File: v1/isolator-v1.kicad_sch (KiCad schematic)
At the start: 43 parts, among them J1 HOST, J2 PORT, Q1 2N7002, T1 750313638, U1 ADuM4165, U2 USBLC6-2SC6, U3 USBLC6-2SC6, U4 SN6505BDBV, U5 TLV76750DGNR, U6 TPS2553DBV, Y1 24M 8pF

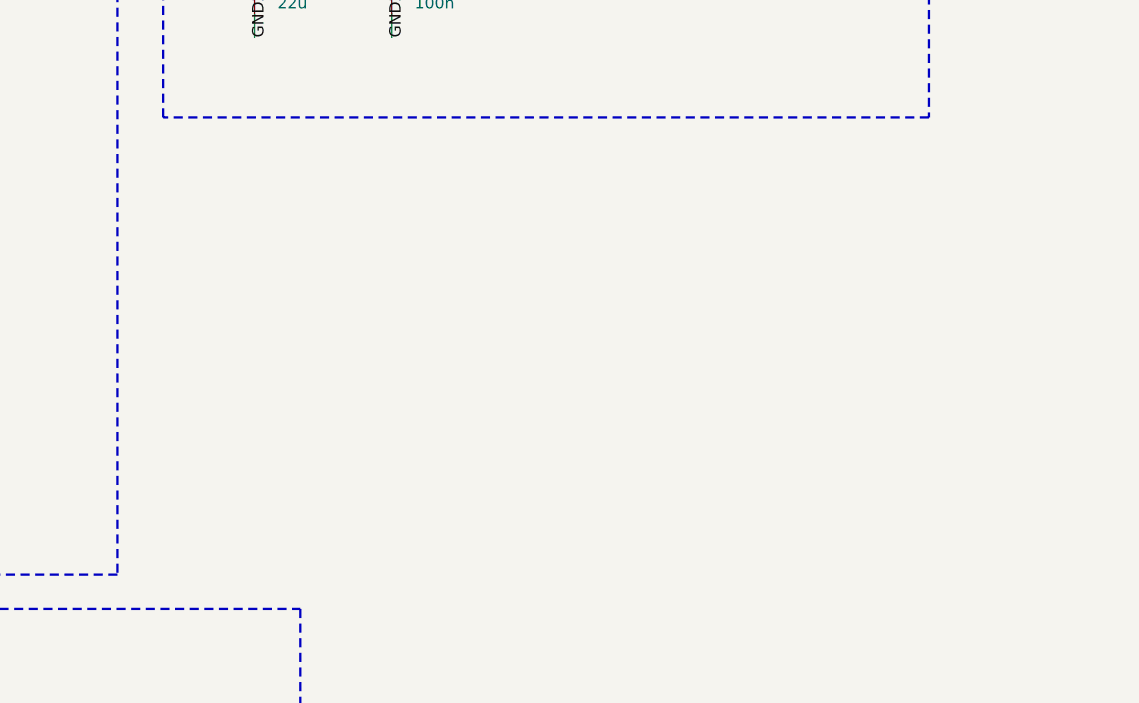
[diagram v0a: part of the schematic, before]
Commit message: feat(v1/sch): footprint audit and binding layout constraints (Task 7)
Audited all 43 v1 component instances: every symbol already carried the
correct footprint from Tasks 2-6 (no reassignment needed). Verified all 15
distinct footprints resolve to real files on disk (stock KiCad libraries +
isolator-lib.pretty), not just non-empty strings.

Added the "V1 LAYOUT CONSTRAINTS -- BINDING" text block to previously-empty
sheet space so the PCB plan inherits the 7 binding constraints (edge
pullback, ESD placement, barrier creepage, bypass lead length, connector
mounting, and the 1.7 mm length-chain margin / D1+D2 side-by-side
requirement) without needing the spec open.

Mechanical sanity check against the Task 1 feasibility budget found the
rectifier zone's real margin is +0.64 mm, not the +2.64 mm previously
reported -- the feasibility doc's D_SMA dimension was an unmeasured 5.0 mm
placeholder; the real D_SMA footprint is 7.0 mm along the load-bearing
axis. Still GO, but effectively zero slack; flagged for Task 8, no
schematic change needed since the footprint is correct.

Verified: ERC baseline held (0 errors, 1 pre-existing lib_symbol_mismatch
warning on U4), netlist MISSING FOOTPRINTS none, programmatic overlap
sweep (124 text/label items) clean, visual render clean.

Co-Authored-By: Claude Opus 5 <noreply@anthropic.com>
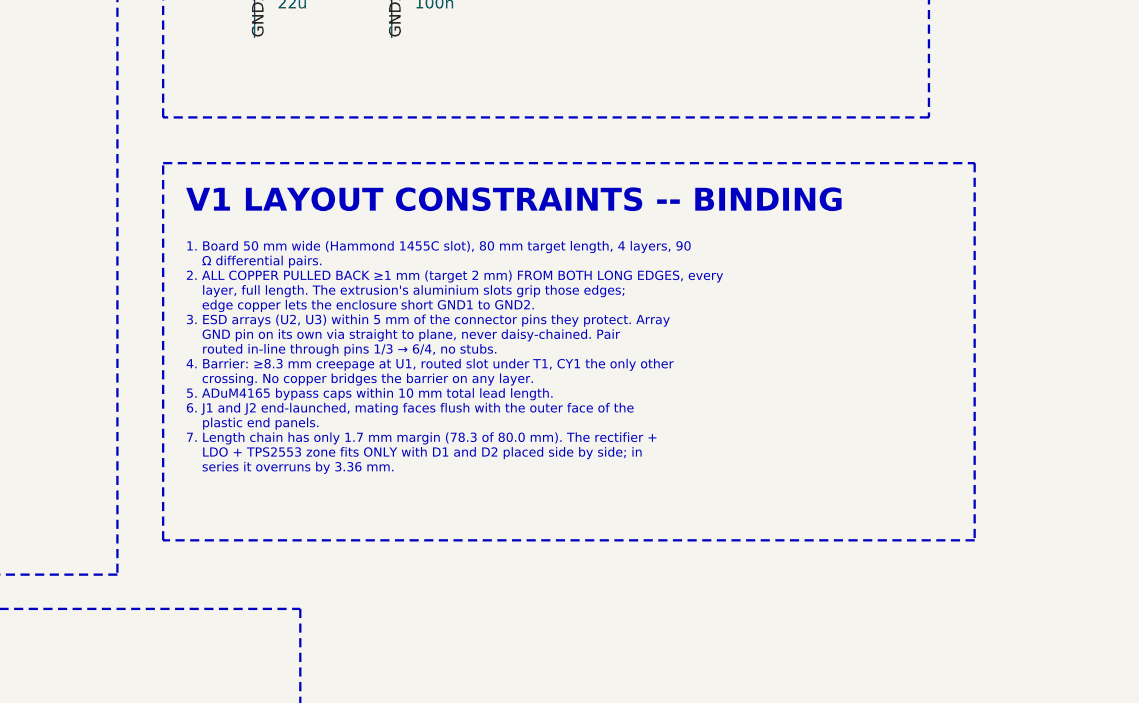
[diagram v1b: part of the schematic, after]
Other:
- note added: "1. Board 50 mm wide (Hammond 1455C slot), 80 mm target length, 4 layers, 90 Ω differential pairs. 2. ALL COPPER PULLED BACK ≥1 mm (target 2 mm) FROM BOTH LONG EDGES, every layer, full length. The extrusion's aluminium slots grip those edges; edge copper lets the enclosure short GND1 to GND2. 3. ESD arrays (U2, U3) within 5 mm of the connector pins they protect. Array GND pin on its own via straig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"
- note added: "V1 LAYOUT CONSTRAINTS -- BINDING"
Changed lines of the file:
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@@
+		)
+	)
+	(rectangle
+		(start 314.96 190.5)
+		(end 405.13 232.41)
+		(stroke
+			(width 0.254)
+			(type dash)
+		)
+		(fill
+			(type none)
+		)
+	)
+	(text "V1 LAYOUT CONSTRAINTS -- BINDING"
+		(exclude_from_sim no)
+		(at 317.5 196.34 0)
+		(effects
+			(font
+				(size 2.54 2.54)
+				(bold yes)
+			)
+			(justify left bottom)
+		)
+	)
+	(text "1. Board 50 mm wide (Hammond 1455C slot), 80 mm target length, 4 layers, 90\n    Ω differential pairs.\n2. ALL COPPER PULLED BACK ≥1 mm (target 2 mm) FROM BOTH LONG EDGES, every\n    layer, full length. The extrusion's aluminium slots grip those edges;\n    edge copper lets the enclosure short GND1 to GND2.\n3. ESD arrays (U2, U3) within 5 mm of the connector pins they protect. Array\n    GND pin on its own via straight to plane, never daisy-chained. Pair\n    routed in-line through pins 1/3 → 6/4, no stubs.\n4. Barrier: ≥8.3 mm creepage at U1, routed slot under T1, CY1 the only other\n    crossing. No copper bridges the barrier on any layer.\n5. ADuM4165 bypass caps within 10 mm total lead length.\n6. J1 and J2 end-launched, mating faces flush with the outer face of the\n    plastic end panels.\n7. Length chain has only 1.7 mm margin (78.3 of 80.0 mm). The rectifier +\n    LDO + TPS2553 zone fits ONLY with D1 and D2 placed side by side; in\n    series it overruns by 3.36 mm."
+		(exclude_from_sim no)
+		(at 317.5 199.39 0)
+		(effects
+			(font
+				(size 1.016 1.016)
+			)
+			(justify left top)
 		)
 	)

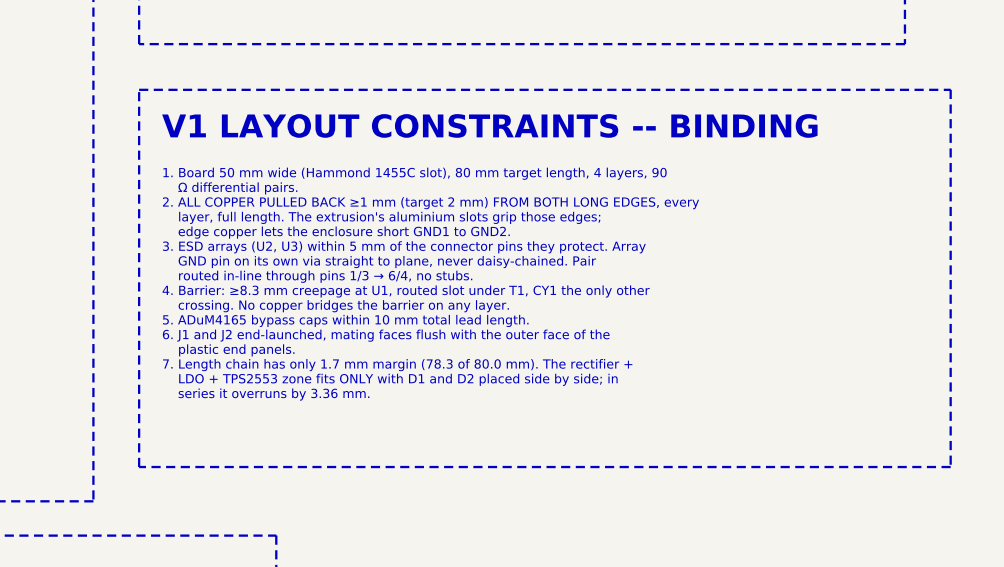
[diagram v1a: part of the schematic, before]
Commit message: docs(v1): move feasibility record to 1455C1202, fix utilization arithmetic (Task 7 fix round 1)
Human partner ruled v1 moves to the 1455C1202 (120 mm) enclosure after the
reviewer extended Task 7's own recompute methodology to zones 1/5 and found
the full 5-zone chain no longer closes against 80 mm (80.1-83.7 mm real vs
80.0 mm available). Spec/plan already updated in 7366d81.

- Schematic constraints text (v1/isolator-v1.kicad_sch): item 1 now reads
  "120 mm length (1455C1202)"; item 7 rewritten to drop the stale 1.7 mm
  margin figure and carry forward only what survives the enclosure change
  -- the rectifier zone measures 19.36 mm and D1/D2 must be placed side by
  side, not in series. Text-only edit, netlist unchanged (verified by diff).

- docs/superpowers/reviews/2026-07-28-v1-mechanical-feasibility.md rewritten
  in full: 120 mm/5520 mm^2 envelope, every one of the 43 BOM components
  measured individually (zero placeholders anywhere, 921.98 mm^2 total,
  16.7% utilization), 5-zone chain recomputed for zones 1/4/5 (80.10-83.70
  mm, reproducing the review's own numbers), zone 2 flagged as a conservative
  hold rather than a re-derived figure, and the 1-D-chain-vs-2-D-board
  caveat carried through so this isn't written up as a hard 80 mm failure.

- Utilization arithmetic error corrected and explained: the previous
  919.6 mm^2/25.0% figure mixed measured and placeholder values
  inconsistently without saying so. Reproduced the review's clean partial
  reconstruction (871.9 mm^2/23.7%) to show where it came from, then
  superseded both with a from-scratch, zero-placeholder recompute.

Re-verified: ERC baseline held (0 errors, 1 pre-existing lib_symbol_mismatch
on U4), netlist identical apart from export timestamp, overlap sweep clean
(124 items), 300 dpi render clean.

Co-Authored-By: Claude Opus 5 <noreply@anthropic.com>
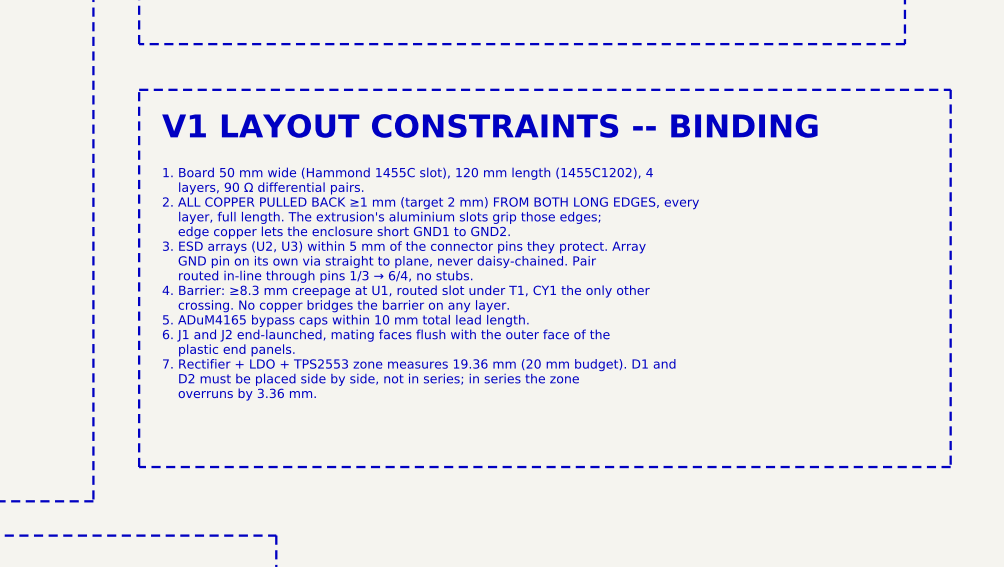
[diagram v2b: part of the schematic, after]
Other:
- note added: "1. Board 50 mm wide (Hammond 1455C slot), 120 mm length (1455C1202), 4 layers, 90 Ω differential pairs. 2. ALL COPPER PULLED BACK ≥1 mm (target 2 mm) FROM BOTH LONG EDGES, every layer, full length. The extrusion's aluminium slots grip those edges; edge copper lets the enclosure short GND1 to GND2. 3. ESD arrays (U2, U3) within 5 mm of the connector pins they protect. Array GND pin on its own via 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"
- note removed: "1. Board 50 mm wide (Hammond 1455C slot), 80 mm target length, 4 layers, 90 Ω differential pairs. 2. ALL COPPER PULLED BACK ≥1 mm (target 2 mm) FROM BOTH LONG EDGES, every layer, full length. The extrusion's aluminium slots grip those edges; edge copper lets the enclosure short GND1 to GND2. 3. ESD arrays (U2, U3) within 5 mm of the connector pins they protect. Array GND pin on its own via straig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"
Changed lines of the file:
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@@
 		)
 	)
-	(text "1. Board 50 mm wide (Hammond 1455C slot), 80 mm target length, 4 layers, 90\n    Ω differential pairs.\n2. ALL COPPER PULLED BACK ≥1 mm (target 2 mm) FROM BOTH LONG EDGES, every\n    layer, full length. The extrusion's aluminium slots grip those edges;\n    edge copper lets the enclosure short GND1 to GND2.\n3. ESD arrays (U2, U3) within 5 mm of the connector pins they protect. Array\n    GND pin on its own via straight to plane, never daisy-chained. Pair\n    routed in-line through pins 1/3 → 6/4, no stubs.\n4. Barrier: ≥8.3 mm creepage at U1, routed slot under T1, CY1 the only other\n    crossing. No copper bridges the barrier on any layer.\n5. ADuM4165 bypass caps within 10 mm total lead length.\n6. J1 and J2 end-launched, mating faces flush with the outer face of the\n    plastic end panels.\n7. Length chain has only 1.7 mm margin (78.3 of 80.0 mm). The rectifier +\n    LDO + TPS2553 zone fits ONLY with D1 and D2 placed side by side; in\n    series it overruns by 3.36 mm."
+	(text "1. Board 50 mm wide (Hammond 1455C slot), 120 mm length (1455C1202), 4\n    layers, 90 Ω differential pairs.\n2. ALL COPPER PULLED BACK ≥1 mm (target 2 mm) FROM BOTH LONG EDGES, every\n    layer, full length. The extrusion's aluminium slots grip those edges;\n    edge copper lets the enclosure short GND1 to GND2.\n3. ESD arrays (U2, U3) within 5 mm of the connector pins they protect. Array\n    GND pin on its own via straight to plane, never daisy-chained. Pair\n    routed in-line through pins 1/3 → 6/4, no stubs.\n4. Barrier: ≥8.3 mm creepage at U1, routed slot under T1, CY1 the only other\n    crossing. No copper bridges the barrier on any layer.\n5. ADuM4165 bypass caps within 10 mm total lead length.\n6. J1 and J2 end-launched, mating faces flush with the outer face of the\n    plastic end panels.\n7. Rectifier + LDO + TPS2553 zone measures 19.36 mm (20 mm budget). D1 and\n    D2 must be placed side by side, not in series; in series the zone\n    overruns by 3.36 mm."
 		(exclude_from_sim no)
 		(at 317.5 199.39 0)

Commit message: feat(v1/sch): MPNs, BOM export, schematic design review
Closes the two named BOM gaps (C3/C7 4.7uF, C8/C10 47uF) with live-verified
LCSC parts, and verifies R3-R8/R9/R10/U5 LCSC codes against the live
catalogue. Exports the BOM (25 lines, 100% MPN coverage), runs the
kicad-happy analyzer, and walks the v1 spec point by point against the
exported netlist (8/8 satisfied, 0 deviations). All 6 non-info analyzer
findings triaged as false positives of one root cause (PWR_FLAG not
recognized as a net source), already identified and accepted in Task 6.
ERC unchanged from baseline: 0 errors, 1 pre-existing lib_symbol_mismatch
warning on U4, not touched per prior direction.

Co-Authored-By: Claude Opus 5 <noreply@anthropic.com>
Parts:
- C10, C8: LCSC (none) -> C90142; MPN (none) -> TMK325ABJ476MM-P; Manufacturer (none) -> Taiyo Yuden
- C3, C7: LCSC (none) -> C162427; MPN (none) -> GRM21BR71E475KA73L; Manufacturer (none) -> Murata
- R10, R4, R9: LCSC (none) -> C14675
- R3: LCSC (none) -> C273780
- R5: LCSC (none) -> C105881
- R6: LCSC (none) -> C137732
- R7, R8: LCSC (none) -> C114630
- U5: LCSC (none) -> C3752807
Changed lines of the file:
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@@
 			)
 		)
+		(property "MPN" "GRM21BR71E475KA73L"
+			(at 25.4 49.53 0)
+			(show_name no)
+			(do_not_autoplace no)
+		(hide yes)
+			(effects
+				(font
+					(size 1.27 1.27)
+				)
+			)
+		)
+		(property "Manufacturer" "Murata"
+			(at 25.4 49.53 0)
+			(show_name no)
+			(do_not_autoplace no)
+		(hide yes)
+			(effects
+				(font
+					(size 1.27 1.27)
+				)
+			)
+		)
+		(property "LCSC" "C162427"
+			(at 25.4 49.53 0)
+			(show_name no)
+			(do_not_autoplace no)
+		(hide yes)
+			(effects
+				(font
+					(size 1.27 1.27)
+				)
+			)
+		)
 		(pin "1"
 		)
@@
 			)
 		)
+		(property "MPN" "GRM21BR71E475KA73L"
+			(at 38.1 130.81 0)
+			(show_name no)
+			(do_not_autoplace no)
+		(hide yes)
+			(effects
+				(font
+					(size 1.27 1.27)
+				)
+			)
+		)
+		(property "Manufacturer" "Murata"
+			(at 38.1 130.81 0)
+			(show_name no)
+			(do_not_autoplace no)
+		(hide yes)
+			(effects
+				(font
+					(size 1.27 1.27)
+				)
+			)
+		)
+		(property "LCSC" "C162427"
+			(at 38.1 130.81 0)
+			(show_name no)
+			(do_not_autoplace no)
+		(hide yes)
+			(effects
+				(font
+					(size 1.27 1.27)
+				)
+			)
+		)
 		(pin "1"
 		)
@@
 			)
 		)
+		(property "MPN" "TMK325ABJ476MM-P"
+			(at 222.25 135.89 0)
+			(show_name no)
+			(do_not_autoplace no)
+		(hide yes)
+			(effects
+				(font
+					(size 1.27 1.27)
+				)
+			)
+		)
+		(property "Manufacturer" "Taiyo Yuden"
+			(at 222.25 135.89 0)
+			(show_name no)
+			(do_not_autoplace no)
+		(hide yes)
+			(effects
+				(font
+					(size 1.27 1.27)
+				)
+			)
+		)
+		(property "LCSC" "C90142"
+			(at 222.25 135.89 0)
+			(show_name no)
+			(do_not_autoplace no)
+		(hide yes)
+			(effects
+				(font
+					(size 1.27 1.27)
+				)
+			)
+		)
 		(pin "1"
 		)
@@
 			)
 		)
+		(property "LCSC" "C3752807"
+			(at 260.35 135.89 0)
+			(show_name no)
+			(do_not_autoplace no)
+		(hide yes)
+			(effects
+				(font
+					(size 1.27 1.27)
+				)
+			)
+		)
 		(property "MPN" "TLV76750DGNR"
 			(at 260.35 135.89 0)
@@
 			)
 		)
+		(property "MPN" "TMK325ABJ476MM-P"
+			(at 283.21 135.89 0)
+			(show_name no)
+			(do_not_autoplace no)
+		(hide yes)
+			(effects
+				(font
+					(size 1.27 1.27)
+				)
+			)
+		)
+		(property "Manufacturer" "Taiyo Yuden"
+			(at 283.21 135.89 0)
+			(show_name no)
+			(do_not_autoplace no)
+		(hide yes)
+			(effects
+				(font
+					(size 1.27 1.27)
+				)
+			)
+		)
+		(property "LCSC" "C90142"
+			(at 283.21 135.89 0)
+			(show_name no)
+			(do_not_autoplace no)
+		(hide yes)
+			(effects
+				(font
+					(size 1.27 1.27)
+				)
+			)
+		)
 		(pin "1"
 		)
@@
 			)
 		)
+		(property "LCSC" "C14675"
+			(at 342.9 77.47 0)
+			(show_name no)
+			(do_not_autoplace no)
+		(hide yes)
+			(effects
+				(font
+					(size 1.27 1.27)
+				)
+			)
+		)
 		(property "MPN" "RC0603FR-07100KL"
 			(at 342.9 77.47 0)
@@
 			)
 		)
+		(property "LCSC" "C14675"
+			(at 353.06 77.47 0)
+			(show_name no)
+			(do_not_autoplace no)
+		(hide yes)
+			(effects
+				(font
+					(size 1.27 1.27)
+				)
+			)
+		)
 		(property "MPN" "RC0603FR-07100KL"
 			(at 353.06 77.47 0)
@@
 			)
 		)
+		(property "LCSC" "C137732"
+			(at 375.92 38.1 0)
+			(show_name no)
+			(do_not_autoplace no)
+		(hide yes)
+			(effects
+				(font
+					(size 1.27 1.27)
+				)
+			)
+		)
 		(property "MPN" "RC0603FR-073K01L"
 			(at 375.92 38.1 0)
@@
 			)
 		)
+		(property "LCSC" "C273780"
+			(at 322.58 127 0)
+			(show_name no)
+			(do_not_autoplace no)
+		(hide yes)
+			(effects
+				(font
+					(size 1.27 1.27)
+				)
+			)
+		)
 		(property "MPN" "RC0603FR-0793K1L"
 			(at 322.58 127 0)
@@
 			)
 		)
+		(property "LCSC" "C14675"
+			(at 365.76 124.46 0)
+			(show_name no)
+			(do_not_autoplace no)
+		(hide yes)
+			(effects
+				(font
+					(size 1.27 1.27)
+				)
+			)
+		)
 		(property "MPN" "RC0603FR-07100KL"
 			(at 365.76 124.46 0)
@@
 			)
 		)
+		(property "LCSC" "C105881"
+			(at 378.46 124.46 0)
+			(show_name no)
+			(do_not_autoplace no)
+		(hide yes)
+			(effects
+				(font
+					(size 1.27 1.27)
+				)
+			)
+		)
 		(property "MPN" "RC0603FR-07330RL"
 			(at 378.46 124.46 0)
@@
 			)
 		)
+		(property "LCSC" "C114630"
+			(at 247.65 187.96 0)
+			(show_name no)
+			(do_not_autoplace no)
+		(hide yes)
+			(effects
+				(font
+					(size 1.27 1.27)
+				)
+			)
+		)
 		(property "MPN" "RC0603FR-0756KL"
 			(at 247.65 187.96 0)
@@
 			(at 262.89 190.5 0)
 			(show_name no)
+			(do_not_autoplace no)
+		(hide yes)
+			(effects
+				(font
+					(size 1.27 1.27)
+				)
+			)
+		)
+		(property "LCSC" "C114630"
+			(at 262.89 190.5 0)
+			(show_name no)
